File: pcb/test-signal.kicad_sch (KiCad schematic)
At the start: 11 parts, among them J5 731000105, U147 SN74LVC1G3157DCKR, U148 AD5683RARMZ

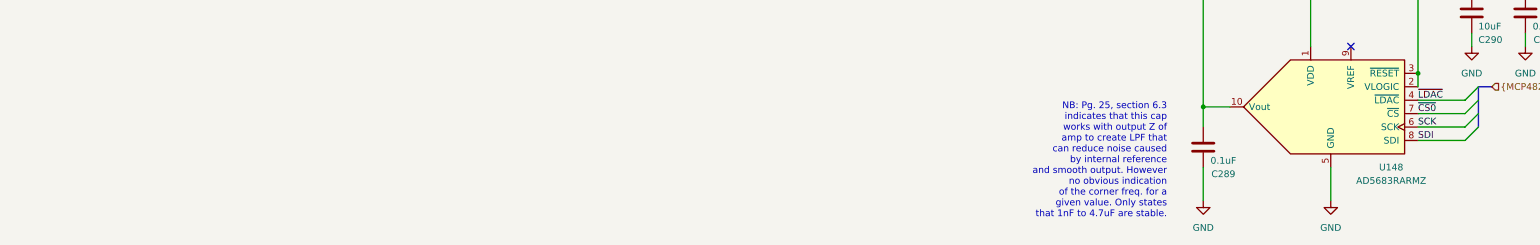
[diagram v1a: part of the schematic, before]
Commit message: Created case
- Mill aluminum
- Moved some components for more sensical layout for the user
- Pending final check, should be ready for initial fab
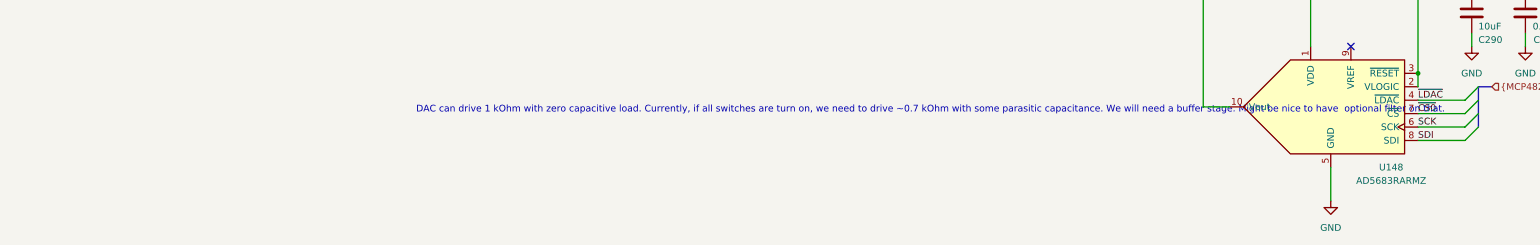
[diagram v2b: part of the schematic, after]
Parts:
- removed C289: 0.1uF, Capacitor_SMD:C_0402_1005Metric, symbol Device:C
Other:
- note added: "DAC can drive 1 kOhm with zero capacitive load. Currently, if all switches are turn on, we need to drive ~0.7 kOhm with some parasitic capacitance. We will need a buffer stage. Might be nice to have optional filter on that."
- note removed: "NB: Pg. 25, section 6.3 indicates that this cap works with output Z of amp to create LPF that can reduce noise caused by internal reference and smooth output. However no obvious indication of the corner freq. for a given value. Only states that 1nF to 4.7uF are stable."
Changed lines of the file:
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@@
-	)
-	(junction
-		(at 127 107.95)
-		(diameter 0)
-		(color 0 0 0 0)
 	)
 	(junction
@@
 	(wire
 		(pts
-			(xy 127 119.38) (xy 127 125.73)
-		)
-		(stroke
-			(width 0)
-			(type default)
-		)
-	)
-	(wire
-		(pts
 			(xy 177.8 86.36) (xy 177.8 83.82)
 		)
@@
 		)
 	)
-	(wire
-		(pts
-			(xy 127 107.95) (xy 127 111.76)
-		)
-		(stroke
-			(width 0)
-			(type default)
-		)
-	)
 	(bus
 		(pts
@@
 		)
 	)
-	(text "NB: Pg. 25, section 6.3\nindicates that this cap\nworks with output Z of\namp to create LPF that\ncan reduce noise caused\nby internal reference\nand smooth output. However\nno obvious indication\nof the corner freq. for a\ngiven value. Only states\nthat 1nF to 4.7uF are stable."
-		(exclude_from_sim no)
-		(at 120.142 129.032 0)
+	(text "DAC can drive 1 kOhm with zero capacitive load. Currently, if all switches are turn on, we need to drive ~0.7 kOhm with some parasitic capacitance. We will need a buffer stage. Might be nice to have  optional filter on that."
+		(exclude_from_sim no)
+		(at 172.72 109.22 0)
 		(effects
 			(font
@@
 	)
 	(symbol
-		(lib_id "power:GND")
-		(at 127 125.73 0)
-		(mirror y)
-		(unit 1)
-		(exclude_from_sim no)
-		(in_bom yes)
-		(on_board yes)
-		(dnp no)
-		(fields_autoplaced yes)
-		(property "Reference" "#PWR0723"
-			(at 127 132.08 0)
-			(effects
-				(font
-					(size 1.27 1.27)
-				)
-				(hide yes)
-			)
-		)
-		(property "Value" "GND"
-			(at 127 130.81 0)
-			(effects
-				(font
-					(size 1.27 1.27)
-				)
-			)
-		)
-		(property "Footprint" ""
-			(at 127 125.73 0)
-			(effects
-				(font
-					(size 1.27 1.27)
-				)
-				(hide yes)
-			)
-		)
-		(property "Datasheet" ""
-			(at 127 125.73 0)
-			(effects
-				(font
-					(size 1.27 1.27)
-				)
-				(hide yes)
-			)
-		)
-		(property "Description" "Power symbol creates a global label with name \"GND\" , ground"
-			(at 127 125.73 0)
-			(effects
-				(font
-					(size 1.27 1.27)
-				)
-				(hide yes)
-			)
-		)
-		(pin "1"
-		)
-		(instances
-			(project "ephys-test-board"
-				(path "/ffaa6ffd-73fa-4da3-9ff1-78fa7369281f/a1b553e6-360f-440c-99f8-5680e9dd5803"
-					(reference "#PWR0723")
-					(unit 1)
-				)
-			)
-		)
-	)
-	(symbol
 		(lib_id "Device:C")
 		(at 187.96 90.17 0)
@@
 			)
 		)
-		(property "Datasheet" "http://ww1.microchip.com/downloads/en/DeviceDoc/22244B.pdf"
+		(property "Datasheet" "https://www.analog.com/media/en/technical-documentation/data-sheets/AD5683R_5682R_5681R_5683.pdf"
 			(at 124.46 110.49 0)
 			(effects
@@
 					(unit 1)
 				)
-			)
-		)
-	)
-	(symbol
-		(lib_id "Device:C")
-		(at 127 115.57 0)
-		(mirror y)
-		(unit 1)
-		(exclude_from_sim no)
-		(in_bom yes)
-		(on_board yes)
-		(dnp no)
-		(property "Reference" "C289"
-			(at 130.81 120.65 0)
-			(effects
-				(font
-					(size 1.27 1.27)
-				)
-			)
-		)
-		(property "Value" "0.1uF"
-			(at 130.81 118.11 0)
-			(effects
-				(font
-					(size 1.27 1.27)
-				)
-			)
-		)
-		(property "Footprint" "Capacitor_SMD:C_0402_1005Metric"
-			(at 126.0348 119.38 0)
-			(effects
-				(font
-					(size 1.27 1.27)
-				)
-				(hide yes)
-			)
-		)
-		(property "Datasheet" "~"
-			(at 127 115.57 0)
-			(effects
-				(font
-					(size 1.27 1.27)
-				)
-				(hide yes)
-			)
-		)
-		(property "Description" "Unpolarized capacitor"
-			(at 127 115.57 0)
-			(effects
-				(font
-					(size 1.27 1.27)
-				)
-				(hide yes)
-			)
-		)
-		(property "TempCo" "X7R"
-			(at 127 115.57 0)
-			(effects
-				(font
-					(size 1.27 1.27)
-				)
-				(hide yes)
-			)
-		)
-		(property "Voltage" ""
-			(at 127 115.57 0)
-			(effects
-				(font
-					(size 1.27 1.27)
-				)
-				(hide yes)
-			)
-		)
-		(pin "1"
-		)
-		(pin "2"
-		)
-		(instances
-			(project "ephys-test-board"
-				(path "/ffaa6ffd-73fa-4da3-9ff1-78fa7369281f/a1b553e6-360f-440c-99f8-5680e9dd5803"
-					(reference "C289")
-					(unit 1)
-				)

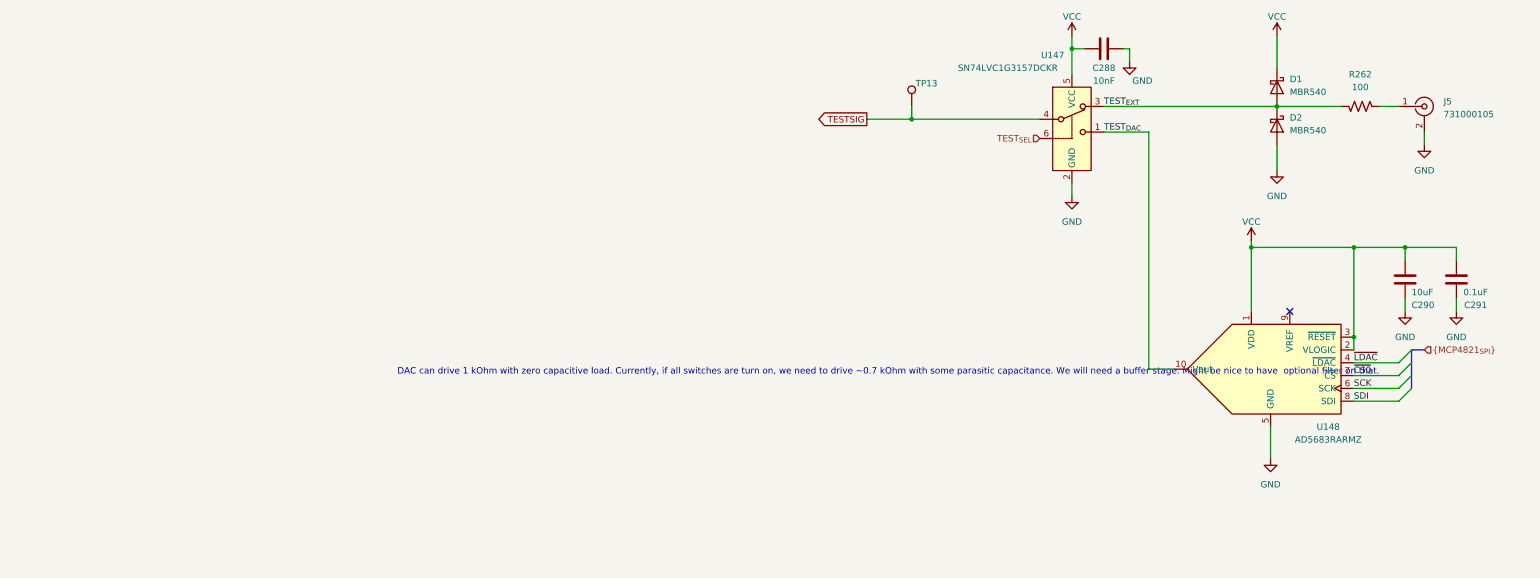
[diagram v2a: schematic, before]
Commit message: Update pdf of schematic
- Additionally, add spice verification of AD5683's
  ability to drive the combined capacitive and
  resistive load presented by the AC coupling
  and attenuation networks
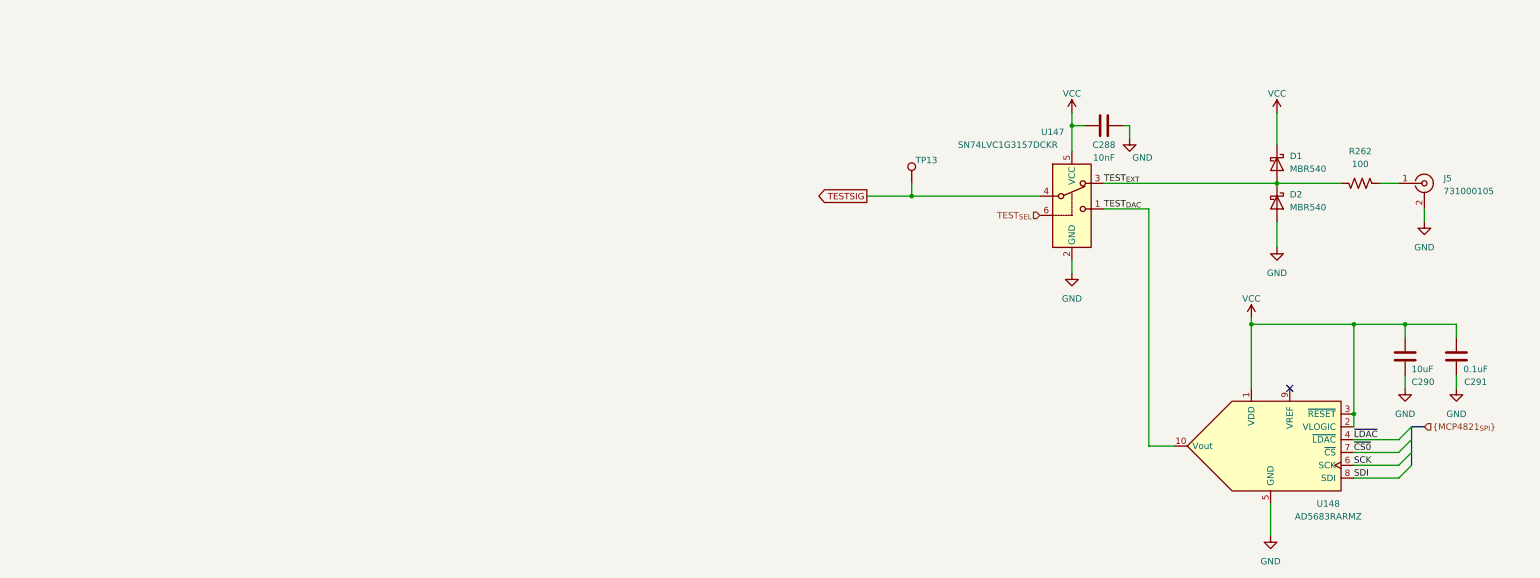
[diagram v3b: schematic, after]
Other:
- note removed: "DAC can drive 1 kOhm with zero capacitive load. Currently, if all switches are turn on, we need to drive ~0.7 kOhm with some parasitic capacitance. We will need a buffer stage. Might be nice to have optional filter on that."
- moved on the sheet: C288, C290, C291, D1, D2, J5, R262, TP13, U147, U148

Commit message: Fix MCP73831 subcircuit
- Add decoupling capacitor on Vbat
- Add more thermal support to layout (solid connection of ground to
  ground plane copper and addition of thermal vias)
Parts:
- D1, D2: value MBR540 -> CDBW140-G
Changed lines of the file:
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@@
 	(title_block
 		(title "Extracellular Electrophysiology Test Board")
-		(rev "A")
+		(rev "B")
 		(company "Open Ephys, Inc")
 		(comment 1 "Jonathan P. Newman")
@@
 			)
 		)
-		(property "Value" "MBR540"
+		(property "Value" "CDBW140-G"
 			(at 154.94 68.2625 90)
 			(effects
@@
 			)
 		)
-		(property "Value" "MBR540"
+		(property "Value" "CDBW140-G"
 			(at 154.94 75.8825 90)
 			(effects

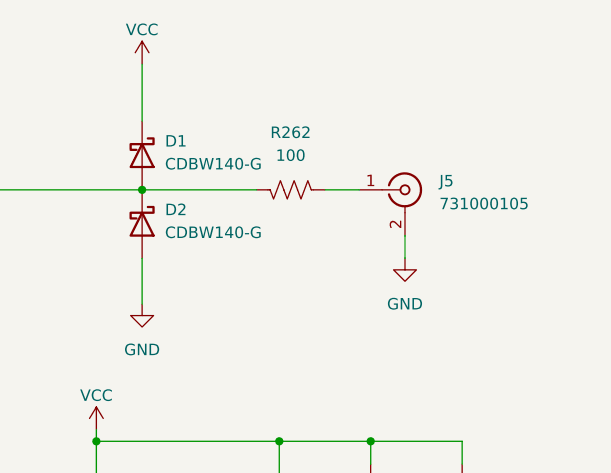
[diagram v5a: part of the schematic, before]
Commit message: Change power switch
- Replace push button with rocker
- Added some notches to outside of PCB for aligning with enclosure
- Upgrade to KiCAD 9.0
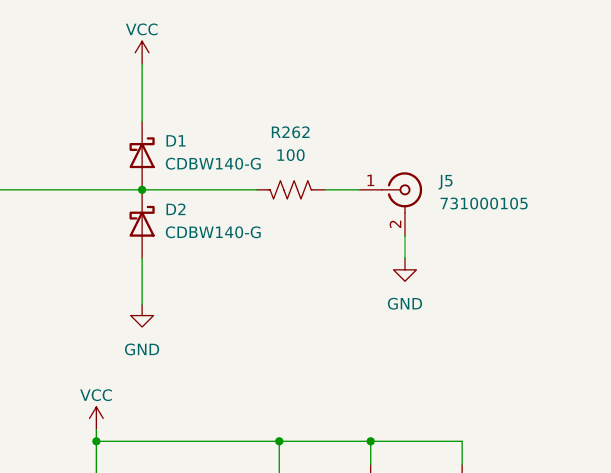
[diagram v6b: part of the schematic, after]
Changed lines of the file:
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@@
 (kicad_sch
-	(version 20231120)
+	(version 20241209)
 	(generator "eeschema")
-	(generator_version "8.0")
+	(generator_version "9.0")
 	(paper "A4")
 	(title_block
@@
 	(label "SCK"
 		(at 167.64 127 0)
-		(fields_autoplaced yes)
 		(effects
 			(font
@@
 	(label "~{CS0}"
 		(at 167.64 124.46 0)
-		(fields_autoplaced yes)
 		(effects
 			(font
@@
 	(label "SDI"
 		(at 167.64 129.54 0)
-		(fields_autoplaced yes)
 		(effects
 			(font
@@
 	(label "TEST_{EXT}"
 		(at 118.11 71.12 0)
-		(fields_autoplaced yes)
 		(effects
 			(font
@@
 	(label "TEST_{DAC}"
 		(at 118.11 76.2 0)
-		(fields_autoplaced yes)
 		(effects
 			(font
@@
 	(label "~{LDAC}"
 		(at 167.64 121.92 0)
-		(fields_autoplaced yes)
 		(effects
 			(font
@@
 		(shape input)
 		(at 181.61 119.38 0)
-		(fields_autoplaced yes)
 		(effects
 			(font
@@
 		(shape input)
 		(at 105.41 77.47 180)
-		(fields_autoplaced yes)
-		(effects
-			(font
+		(effects
+			(font
